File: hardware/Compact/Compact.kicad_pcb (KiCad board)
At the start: 2 copper layers, 40.6 x 18.9 mm, 50 parts, among them J2 Battery, J3 GPIO, J4 USB_B_Micro, J6 LEDs, J7 GPIO, Q1 BSS806N, Q2 BSS806N, Q3 BSS806N, Q4 BSS806N, SW1 Mode, SW2 Power, U1 STM32F411CE, U2 AP2210N-3.3TRG1, U3 MCP73831T-2ACI_OT, U5 GD25Q16CEIGR, Y1 24Mhz

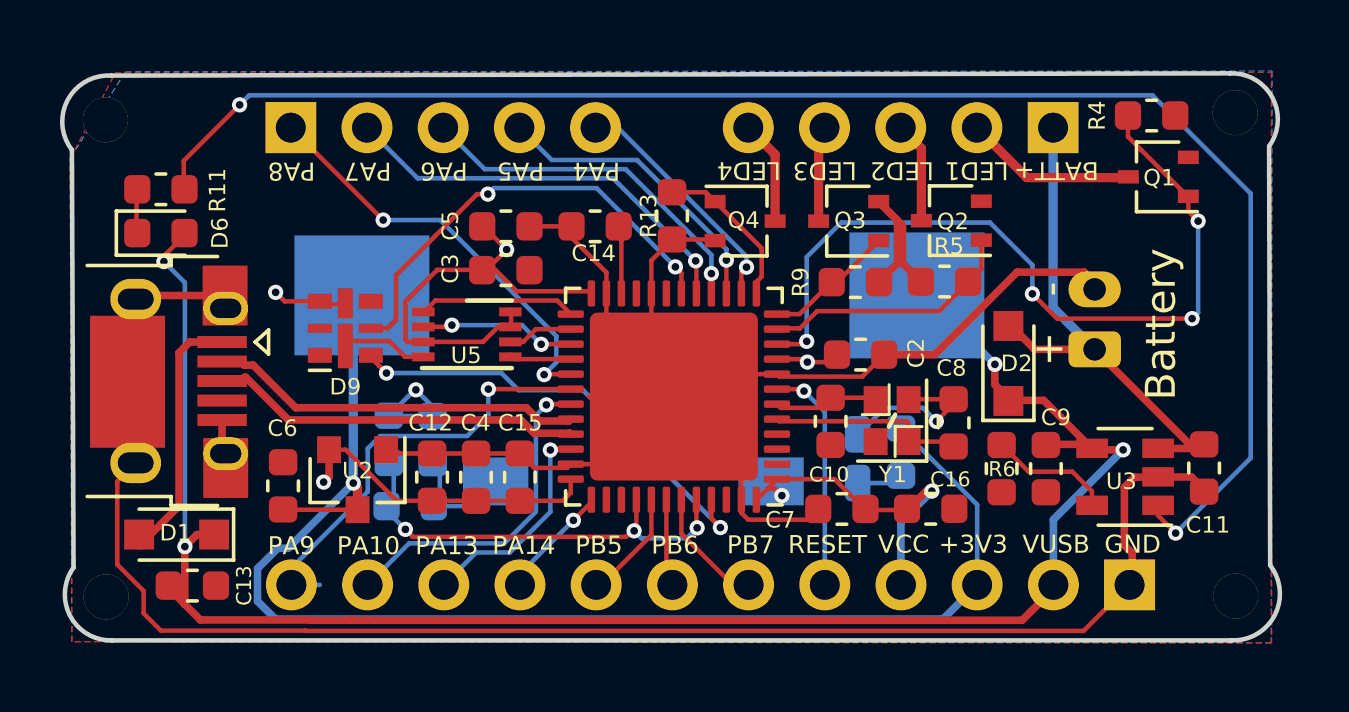
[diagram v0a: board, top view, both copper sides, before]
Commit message: Update switch footprint.
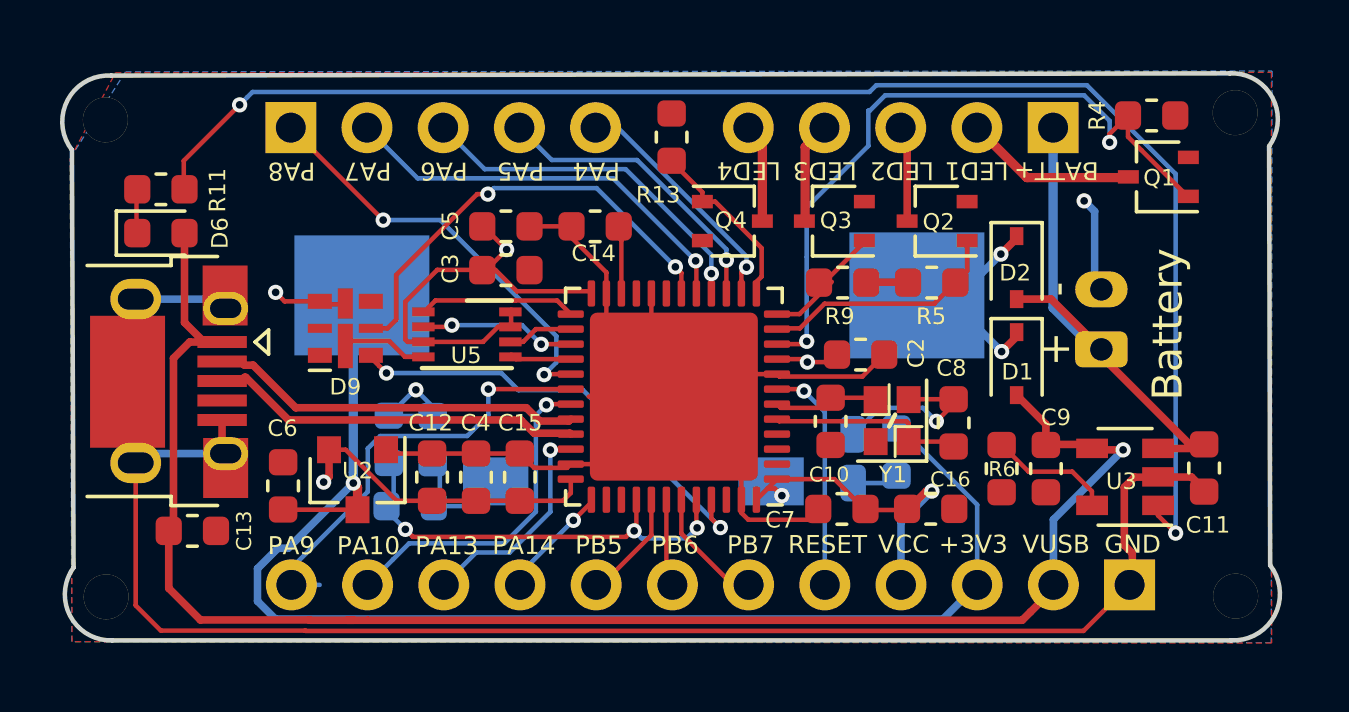
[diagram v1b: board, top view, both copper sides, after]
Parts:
- D1, D2: footprint Diode_SMD:D_SOD-323_HandSoldering -> Diode_SMD:D_SOD-323
- R1: value 270 -> 330
- R6: value 680 -> 2k
- SW1: footprint Jeremy Button/Switch:SW_SPST_FSMSM -> Button_Switch_SMD:SW_SPST_FSMSM
- SW2: footprint Jeremy Button/Switch:SW_LG-15F -> Jeremy:Switch_LG-15F_SMD
- moved D1 28.6 mm to (157.1, 99.3), turned to 270 degrees
- moved D2 3.21 mm to (157.1, 96.1), turned to 270 degrees
- moved R13 2.63 mm to (145.6, 91.8), turned to 90 degrees
- moved C13 1.82 mm to (129.6, 104.9)
- moved Q2 0.48 mm to (154.4, 94.6)
- moved Q3 0.47 mm to (151.0, 94.6)
- moved R5 0.43 mm to (154.2, 96.6)
- moved R9 0.43 mm to (151.3, 96.6)
- moved Q4 0.43 mm to (147.6, 94.6)
- moved J2 0.22 mm to (159.9, 98.8)
- moved D3 0.15 mm to (151.6, 102.5)
- moved R1 0.15 mm to (153.1, 102.3)
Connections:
- D1 pad 1: /VUSB -> Net-(D1-Pad1)
- D1 pad 2: Net-(D1-Pad2) -> /VUSB
- D2 pad 1: /VUSB -> Net-(D1-Pad1)
- J4 pad 1: Net-(D1-Pad2) -> /VUSB
- SW2 pad 1: /VUSB -> Net-(D1-Pad1)
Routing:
- net GND: track 125.8 -> 114.4 mm, vias 2 -> 3
- net Net-(D1-Pad1): track 0.00 -> 8.65 mm, vias 0 -> 2
- net Net-(D1-Pad2): track 8.57 -> 0.00 mm
- net /VUSB: track 61.2 -> 55.0 mm, vias 4 -> 1
- net /LED1: track 26.8 -> 23.6 mm, vias 4 -> 2
- net Net-(R11-Pad2): track 52.4 -> 49.5 mm
- net /LED4: track 5.41 -> 6.00 mm
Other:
- board text added: "ThunderPack v1.2"
- board text removed: "ThunderPack v2"

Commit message: Checkpoint commit (v1.2a3)
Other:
- board text added: "3v3"
- board text removed: "+3V3"

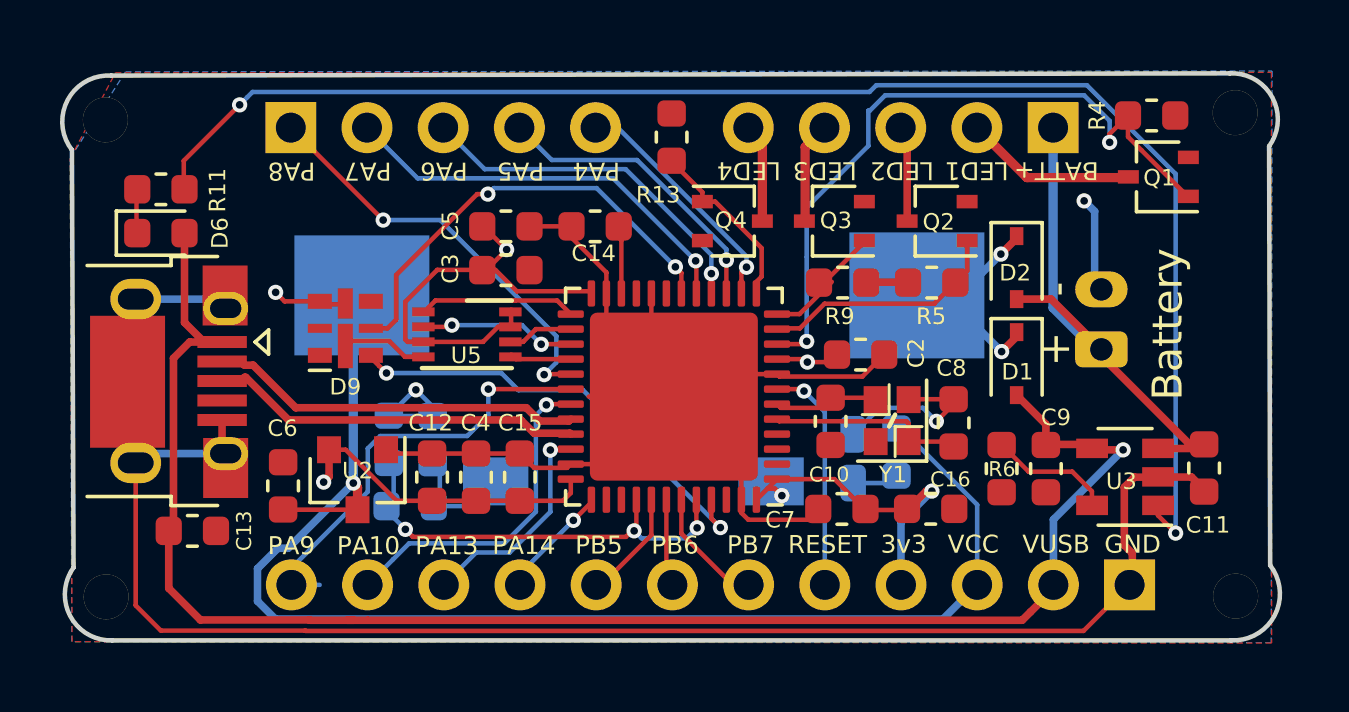
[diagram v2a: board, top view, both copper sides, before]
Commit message: Add 4 PWM LEDs.
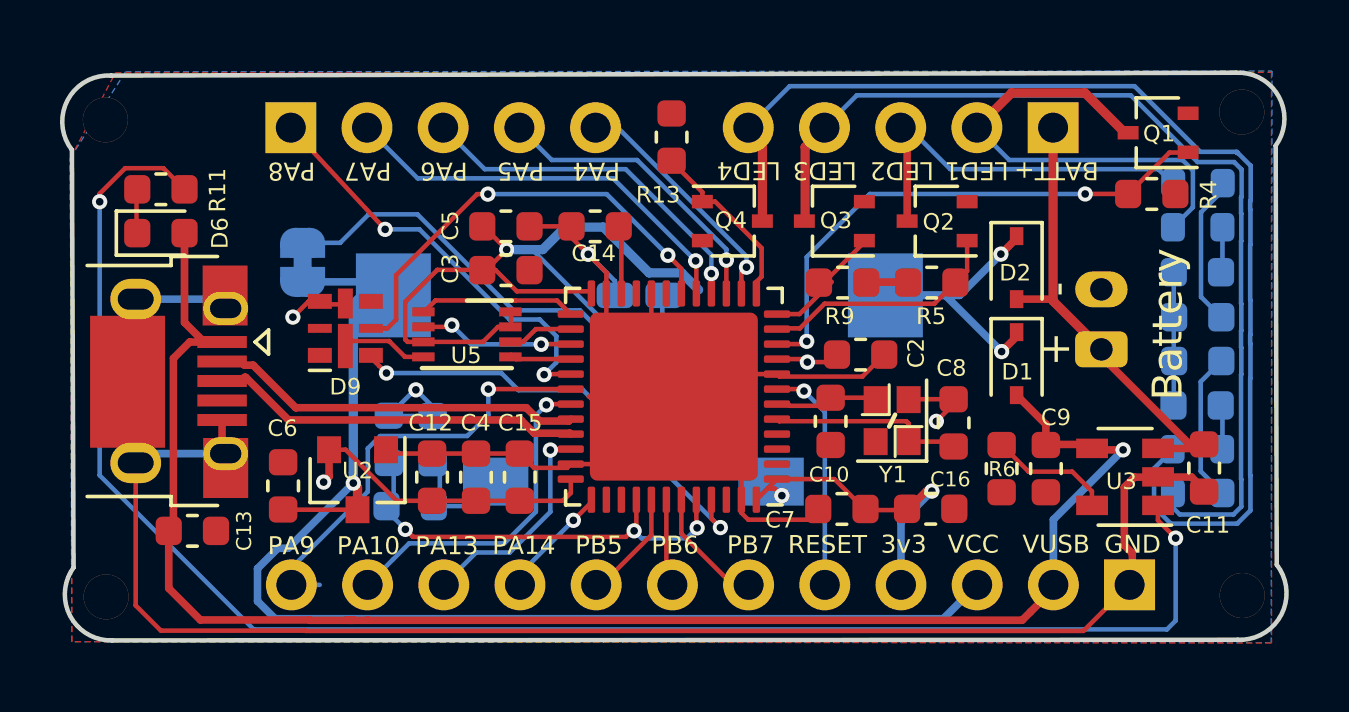
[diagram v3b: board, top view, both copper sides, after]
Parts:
- removed the REF** at (164.4, 107.1)
- removed the REF** at (164.4, 91.0)
- added 1: LED, LED_SMD:LED_0603_1608Metric, B.Cu at (163.1, 96.3)
- added 2: LED, LED_SMD:LED_0603_1608Metric, B.Cu at (163.1, 97.8)
- added 3: LED, LED_SMD:LED_0603_1608Metric, B.Cu at (163.1, 99.2)
- added 4: LED, LED_SMD:LED_0603_1608Metric, B.Cu at (163.1, 100.7)
- added JP1: Jumper, Jumper:SolderJumper-2_P1.3mm_Bridged_RoundedPad1.0x1.5mm, B.Cu at (133.3, 96.0)
- added R10: 270, Resistor_SMD:R_0603_1608Metric, B.Cu at (163.1, 103.6)
- added R12: 270, Resistor_SMD:R_0603_1608Metric, B.Cu at (163.1, 102.2)
- added R7: 270, Resistor_SMD:R_0603_1608Metric, B.Cu at (163.1, 94.8)
- added R8: 270, Resistor_SMD:R_0603_1608Metric, B.Cu at (163.1, 93.3)
- added REF**: 1.5mm-Hole, Jeremy:1.5mm-Hole, F.Cu at (164.6, 107.1)
- added REF**: 1.5mm-Hole, Jeremy:1.5mm-Hole, F.Cu at (164.6, 90.9)
- SW2: footprint Jeremy:Switch_LG-15F_SMD -> Jeremy Button/Switch:SW_KAN-15_SMD
- moved R1 9.40 mm to (144.5, 98.5), turned to 180 degrees
- moved D3 8.97 mm to (144.5, 97.0), turned to 0 degrees
- moved R4 2.62 mm to (161.6, 93.7)
- moved Q1 1.47 mm to (161.8, 91.6)
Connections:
- R1 pad 2: /VIN -> Net-(JP1-Pad2)
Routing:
- net Net-(J6-Pad5): track 3.33 -> 39.1 mm
- net Net-(J6-Pad4): track 3.41 -> 33.1 mm
- net +3V3: track 40.9 -> 59.5 mm
- net Net-(JP1-Pad2): track 0.00 -> 12.5 mm
- net Net-(J6-Pad2): track 5.74 -> 16.0 mm
- net Net-(J6-Pad3): track 3.20 -> 13.1 mm
- net /LED1: track 23.6 -> 18.0 mm
- net Net-(R11-Pad2): track 49.5 -> 55.1 mm
- net Net-(D5-Pad1): track 0.00 -> 5.05 mm
- net Net-(D7-Pad1): track 0.00 -> 4.98 mm
- net GND: track 114.4 -> 109.7 mm
- net /VIN: track 46.7 -> 43.6 mm
- net Net-(D4-Pad1): track 0.00 -> 1.52 mm
- net Net-(D8-Pad1): track 0.00 -> 1.48 mm
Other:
- board size 40.6 x 18.9 mm -> 40.8 x 18.9 mm
- board text added: "PWR LED"
- board text added: "ThunderPack v1.2a3"
- board text removed: "ThunderPack v1.2"

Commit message: Circuit updates
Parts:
- D9: footprint LED_SMD:LED-APA102-2020 -> Jeremy LEDs:LED-APA102-2020
- R10, R12, R7, R8: value 270 -> 330

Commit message: Rename Standard -> Original
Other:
- board text added: "ThunderPack v1.2"
- board text removed: "ThunderPack v1.2a3"

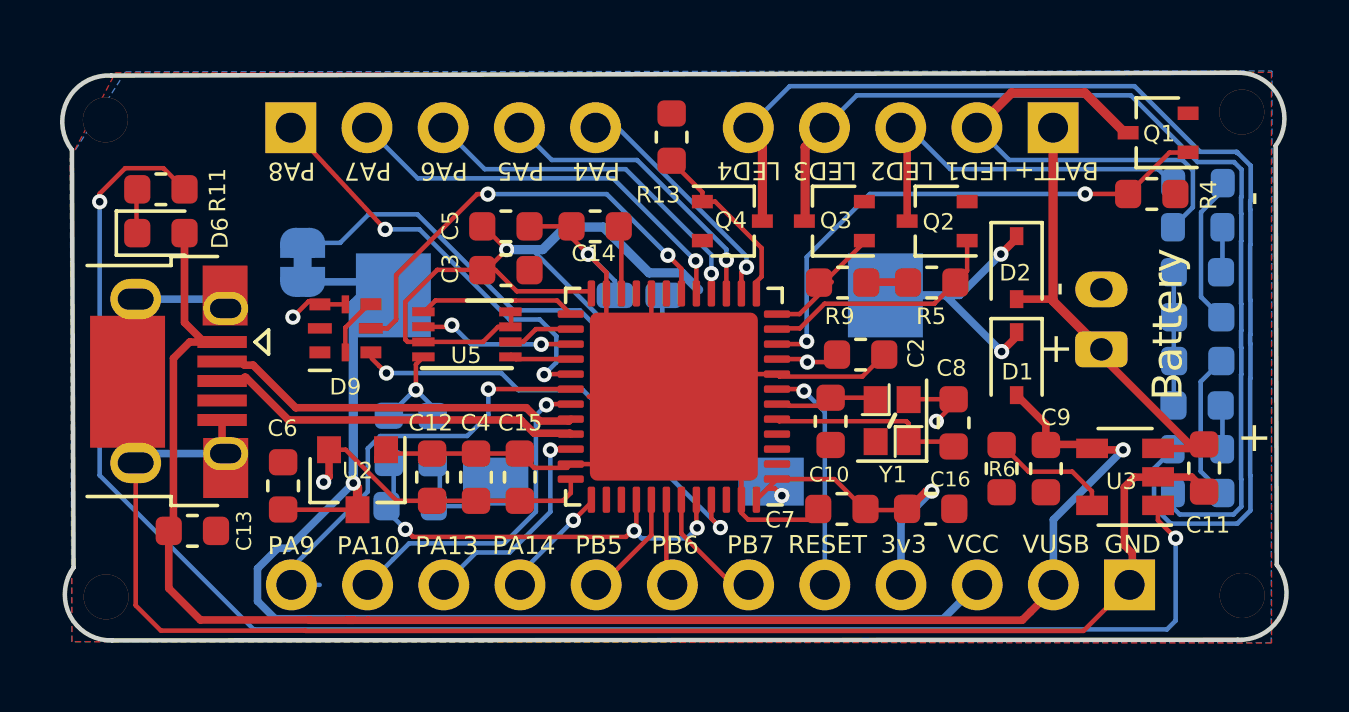
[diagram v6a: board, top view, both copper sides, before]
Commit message: Add ESD. Update labeling
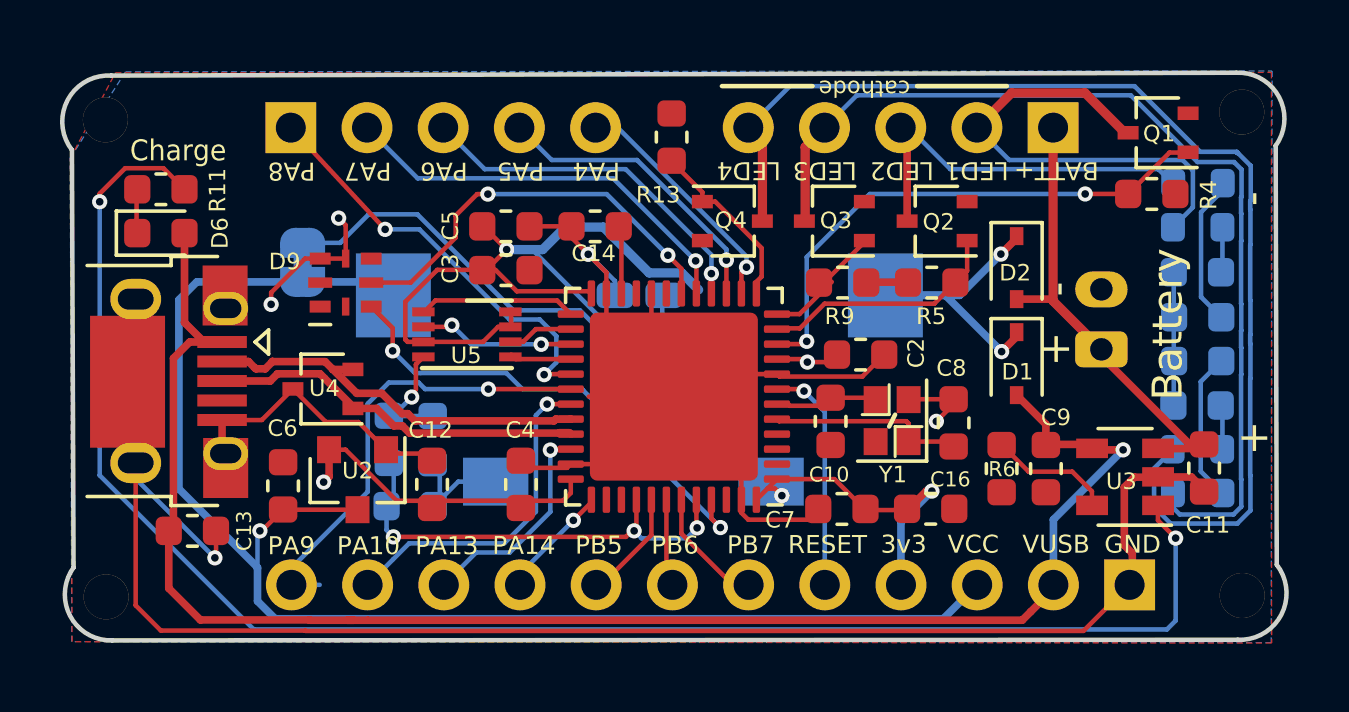
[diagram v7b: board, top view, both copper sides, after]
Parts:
- removed C15: 100nF, Capacitor_SMD:C_0603_1608Metric
- added U4: ESD7002WTT1G, Package_TO_SOT_SMD:SOT-323_SC-70, F.Cu at (133.9, 100.2)
- moved D9 1.53 mm to (134.7, 96.6)
- moved C4 1.51 mm to (140.6, 103.3)
- moved C12 0.24 mm to (137.6, 103.3)
- renumbered 1 to D4, 2 to D5, 3 to D7, 4 to D8
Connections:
- D9 pad 2: (no net) -> Net-(D9-Pad2)
- D9 pad 3: (no net) -> Net-(D9-Pad3)
- J4 pad 4: (no net) -> Net-(J4-Pad4)
- U1 pad 19: (no net) -> Net-(U1-Pad19)
- U1 pad 2: (no net) -> Net-(U1-Pad2)
- U1 pad 21: (no net) -> Net-(U1-Pad21)
- U1 pad 3: (no net) -> Net-(U1-Pad3)
- U1 pad 38: (no net) -> Net-(U1-Pad38)
- U1 pad 39: (no net) -> Net-(U1-Pad39)
- U1 pad 4: (no net) -> Net-(U1-Pad4)
- U1 pad 46: (no net) -> Net-(U1-Pad46)
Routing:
- net GND: track 110.0 -> 115.2 mm, vias 3 -> 4
- net /VIN: track 43.6 -> 48.6 mm
- net +3V3: track 59.5 -> 62.3 mm, vias 6 -> 7
- net /RGB_SDI: track 15.0 -> 16.3 mm
- net /RGB_CKI: track 14.9 -> 13.8 mm
- net /USB_D-: track 12.5 -> 13.4 mm
- net /PA9: track 15.6 -> 16.1 mm
- net /BUTTON: track 14.7 -> 15.2 mm
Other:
- board text added: "1"
- board text added: "2"
- board text added: "3"
- board text added: "4"
- board text added: "Charge"
- board text added: "cathode"

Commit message: Cleanup fills and labels.
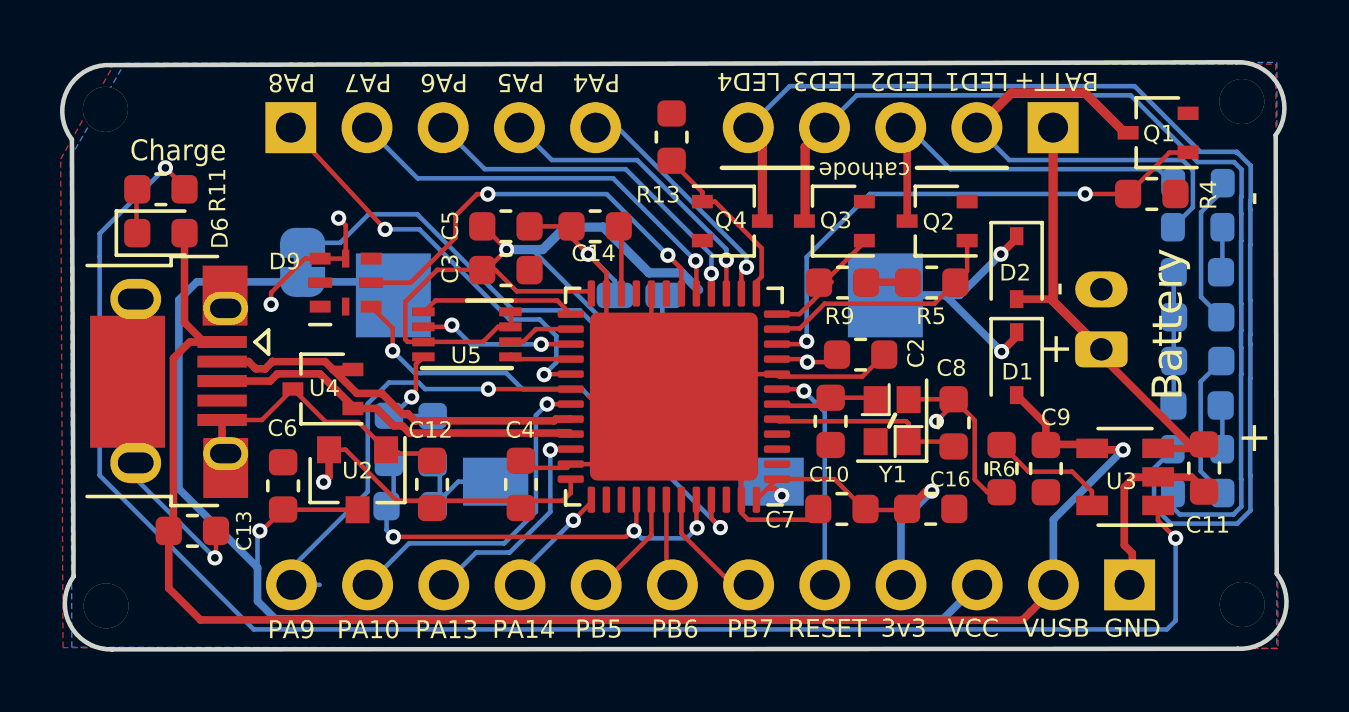
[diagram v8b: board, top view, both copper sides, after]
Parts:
- removed the REF** at (126.7, 107.1)
- removed the REF** at (164.6, 107.1)
- removed the REF** at (126.7, 91.2)
- removed the REF** at (164.6, 90.9)
- added REF**: 1.5mm-Hole, Jeremy:1.5mm-Hole, F.Cu at (126.7, 107.4)
- added REF**: 1.5mm-Hole, Jeremy:1.5mm-Hole, F.Cu at (164.6, 107.4)
- added REF**: 1.5mm-Hole, Jeremy:1.5mm-Hole, F.Cu at (126.7, 90.8)
- added REF**: 1.5mm-Hole, Jeremy:1.5mm-Hole, F.Cu at (164.6, 90.6)
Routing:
- net GND: track 115.2 -> 80.4 mm
- net Net-(R11-Pad2): track 55.1 -> 54.3 mm
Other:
- board size 40.8 x 18.9 mm -> 40.8 x 19.6 mm
